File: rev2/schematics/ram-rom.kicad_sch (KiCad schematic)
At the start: 7 parts, among them U10 28C256, U11 28C256, U12 MT16D832

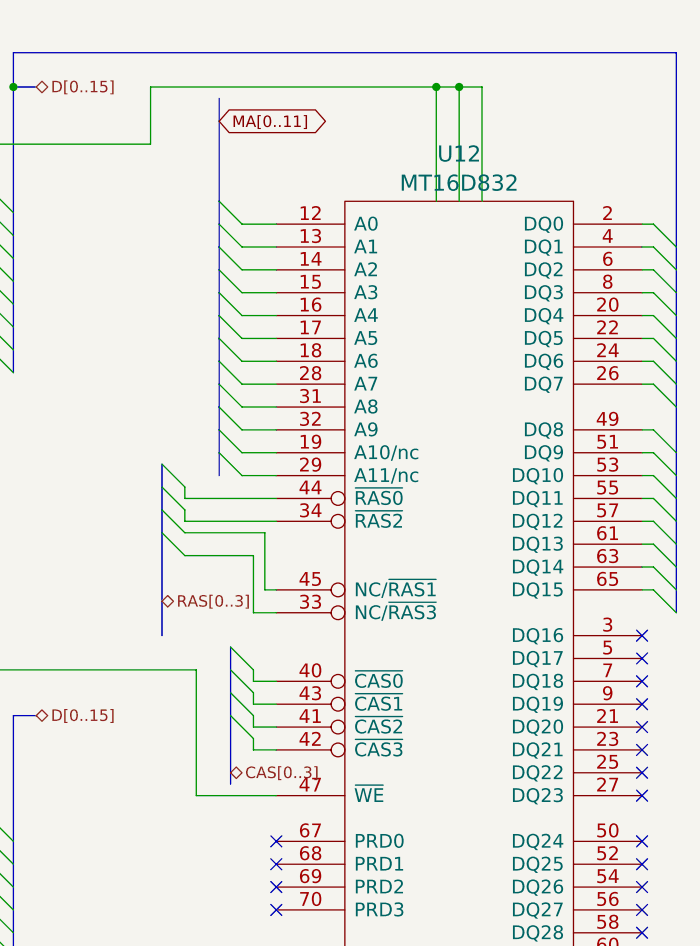
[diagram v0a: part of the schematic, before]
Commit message: Fixed Bus connections. Added SIMM control connections to the CPLD. Added missing symbols from rev1 library. Cleaned up some SRAM related control signals that are no longer needed.
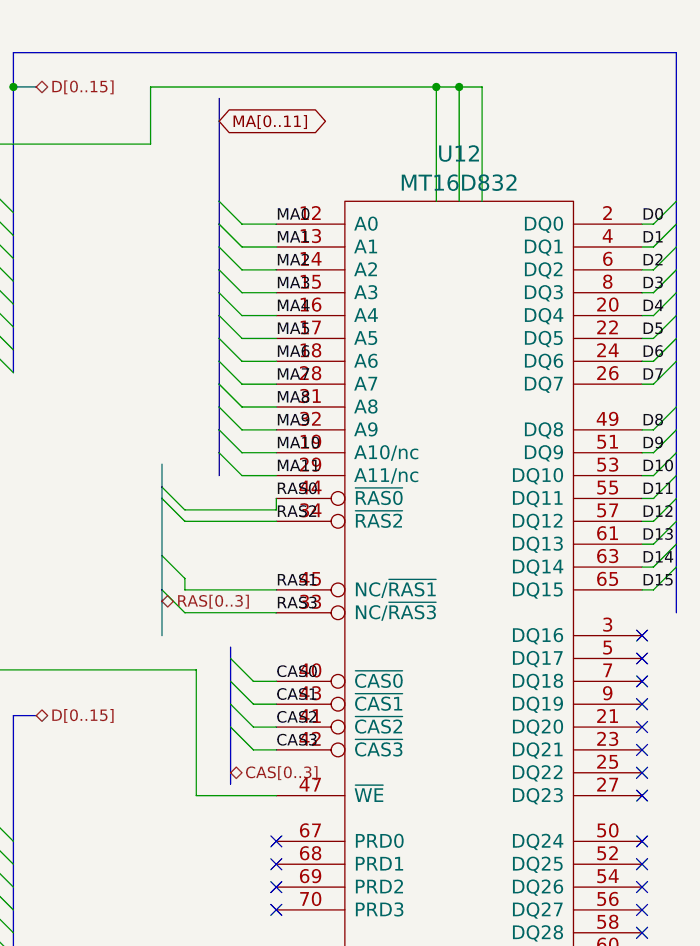
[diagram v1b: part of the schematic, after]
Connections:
- net D0: now also U12.2 (DQ0)
- net D1: now also U12.4 (DQ1)
- net D10: now also U12.53 (DQ10)
- net D11: now also U12.55 (DQ11)
- net D12: now also U12.57 (DQ12)
- net D13: now also U12.61 (DQ13)
- net D14: now also U12.63 (DQ14)
- net D15: now also U12.65 (DQ15)
- net D2: now also U12.6 (DQ2)
- net D3: now also U12.8 (DQ3)
- net D4: now also U12.20 (DQ4)
- net D5: now also U12.22 (DQ5)
- net D6: now also U12.24 (DQ6)
- net D7: now also U12.26 (DQ7)
- net D8: now also U12.49 (DQ8)
- net D9: now also U12.51 (DQ9)
- net MA0: now reaches U12.12 (A0)
- net MA1: now reaches U12.13 (A1)
- net MA2: now reaches U12.14 (A2)
- net MA3: now reaches U12.15 (A3)
- net MA4: now reaches U12.16 (A4)
- net MA5: now reaches U12.17 (A5)
- net MA6: now reaches U12.18 (A6)
- net MA10: now reaches U12.19 (A10/nc)
- net MA7: now reaches U12.28 (A7)
- net MA11: now reaches U12.29 (A11/nc)
- net MA8: now reaches U12.31 (A8)
- net MA9: now reaches U12.32 (A9)
- net RAS3: now reaches U12.33 (NC/~{RAS3})
- net RAS2: now reaches U12.34 (~{RAS2})
- net CAS0: now reaches U12.40 (~{CAS0})
- net CAS2: now reaches U12.41 (~{CAS2})
- net CAS3: now reaches U12.42 (~{CAS3})
- net CAS1: now reaches U12.43 (~{CAS1})
- net RAS0: now reaches U12.44 (~{RAS0})
- net RAS1: now reaches U12.45 (NC/~{RAS1})

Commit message: Added hierarchical labels from main sheet to RAM and ROM sheet.
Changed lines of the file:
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@@
     (effects (font (size 10.0076 10.0076)) (justify left bottom))
   )
-  (label "CAS2" (at 209.55 97.79 0)
+  (label "CAS2" (at 209.55 97.79 0) (fields_autoplaced)
     (effects (font (size 1.27 1.27)) (justify left bottom))
   )
@@
     (effects (font (size 1.27 1.27)) (justify left bottom))
   )
-  (label "MA8" (at 209.55 62.23 0)
+  (label "MA8" (at 209.55 62.23 0) (fields_autoplaced)
     (effects (font (size 1.27 1.27)) (justify left bottom))
   )
@@
     (effects (font (size 1.27 1.27)) (justify left bottom))
   )
-  (label "RAS0" (at 209.55 72.39 0)
-    (effects (font (size 1.27 1.27)) (justify left bottom))
-  )
-  (label "D3" (at 250.19 49.53 0)
-    (effects (font (size 1.27 1.27)) (justify left bottom))
-  )
-  (label "MA0" (at 209.55 41.91 0)
-    (effects (font (size 1.27 1.27)) (justify left bottom))
-  )
-  (label "D15" (at 250.19 82.55 0)
+  (label "RAS0" (at 209.55 72.39 0) (fields_autoplaced)
+    (effects (font (size 1.27 1.27)) (justify left bottom))
+  )
+  (label "D3" (at 250.19 49.53 0) (fields_autoplaced)
+    (effects (font (size 1.27 1.27)) (justify left bottom))
+  )
+  (label "MA0" (at 209.55 41.91 0) (fields_autoplaced)
+    (effects (font (size 1.27 1.27)) (justify left bottom))
+  )
+  (label "D15" (at 250.19 82.55 0) (fields_autoplaced)
     (effects (font (size 1.27 1.27)) (justify left bottom))
   )
@@
     (effects (font (size 1.27 1.27)) (justify left bottom))
   )
-  (label "MA1" (at 209.55 44.45 0)
+  (label "MA1" (at 209.55 44.45 0) (fields_autoplaced)
     (effects (font (size 1.27 1.27)) (justify left bottom))
   )
@@
     (effects (font (size 1.27 1.27)) (justify left bottom))
   )
-  (label "CAS3" (at 209.55 100.33 0)
+  (label "CAS3" (at 209.55 100.33 0) (fields_autoplaced)
     (effects (font (size 1.27 1.27)) (justify left bottom))
   )
@@
     (effects (font (size 1.27 1.27)) (justify left bottom))
   )
-  (label "MA10" (at 209.55 67.31 0)
+  (label "MA10" (at 209.55 67.31 0) (fields_autoplaced)
     (effects (font (size 1.27 1.27)) (justify left bottom))
   )
@@
     (effects (font (size 1.27 1.27)) (justify left bottom))
   )
-  (label "D14" (at 250.19 80.01 0)
-    (effects (font (size 1.27 1.27)) (justify left bottom))
-  )
-  (label "D12" (at 250.19 74.93 0)
+  (label "D14" (at 250.19 80.01 0) (fields_autoplaced)
+    (effects (font (size 1.27 1.27)) (justify left bottom))
+  )
+  (label "D12" (at 250.19 74.93 0) (fields_autoplaced)
     (effects (font (size 1.27 1.27)) (justify left bottom))
   )
@@
     (effects (font (size 1.27 1.27)) (justify left bottom))
   )
-  (label "D1" (at 250.19 44.45 0)
-    (effects (font (size 1.27 1.27)) (justify left bottom))
-  )
-  (label "D0" (at 250.19 41.91 0)
-    (effects (font (size 1.27 1.27)) (justify left bottom))
-  )
-  (label "MA6" (at 209.55 57.15 0)
+  (label "D1" (at 250.19 44.45 0) (fields_autoplaced)
+    (effects (font (size 1.27 1.27)) (justify left bottom))
+  )
+  (label "D0" (at 250.19 41.91 0) (fields_autoplaced)
+    (effects (font (size 1.27 1.27)) (justify left bottom))
+  )
+  (label "MA6" (at 209.55 57.15 0) (fields_autoplaced)
     (effects (font (size 1.27 1.27)) (justify left bottom))
   )
@@
     (effects (font (size 1.27 1.27)) (justify left bottom))
   )
-  (label "D6" (at 250.19 57.15 0)
-    (effects (font (size 1.27 1.27)) (justify left bottom))
-  )
-  (label "D10" (at 250.19 69.85 0)
-    (effects (font (size 1.27 1.27)) (justify left bottom))
-  )
-  (label "CAS1" (at 209.55 95.25 0)
-    (effects (font (size 1.27 1.27)) (justify left bottom))
-  )
-  (label "D9" (at 250.19 67.31 0)
-    (effects (font (size 1.27 1.27)) (justify left bottom))
-  )
-  (label "MA2" (at 209.55 46.99 0)
+  (label "D6" (at 250.19 57.15 0) (fields_autoplaced)
+    (effects (font (size 1.27 1.27)) (justify left bottom))
+  )
+  (label "D10" (at 250.19 69.85 0) (fields_autoplaced)
+    (effects (font (size 1.27 1.27)) (justify left bottom))
+  )
+  (label "CAS1" (at 209.55 95.25 0) (fields_autoplaced)
+    (effects (font (size 1.27 1.27)) (justify left bottom))
+  )
+  (label "D9" (at 250.19 67.31 0) (fields_autoplaced)
+    (effects (font (size 1.27 1.27)) (justify left bottom))
+  )
+  (label "MA2" (at 209.55 46.99 0) (fields_autoplaced)
     (effects (font (size 1.27 1.27)) (justify left bottom))
   )
@@
     (effects (font (size 1.27 1.27)) (justify left bottom))
   )
-  (label "D7" (at 250.19 59.69 0)
+  (label "D7" (at 250.19 59.69 0) (fields_autoplaced)
     (effects (font (size 1.27 1.27)) (justify left bottom))
   )
@@
     (effects (font (size 1.27 1.27)) (justify left bottom))
   )
-  (label "CAS0" (at 209.55 92.71 0)
-    (effects (font (size 1.27 1.27)) (justify left bottom))
-  )
-  (label "MA5" (at 209.55 54.61 0)
-    (effects (font (size 1.27 1.27)) (justify left bottom))
-  )
-  (label "MA7" (at 209.55 59.69 0)
+  (label "CAS0" (at 209.55 92.71 0) (fields_autoplaced)
+    (effects (font (size 1.27 1.27)) (justify left bottom))
+  )
+  (label "MA5" (at 209.55 54.61 0) (fields_autoplaced)
+    (effects (font (size 1.27 1.27)) (justify left bottom))
+  )
+  (label "MA7" (at 209.55 59.69 0) (fields_autoplaced)
     (effects (font (size 1.27 1.27)) (justify left bottom))
   )
@@
     (effects (font (size 1.27 1.27)) (justify left bottom))
   )
-  (label "D2" (at 250.19 46.99 0)
+  (label "D2" (at 250.19 46.99 0) (fields_autoplaced)
     (effects (font (size 1.27 1.27)) (justify left bottom))
   )
@@
     (effects (font (size 1.27 1.27)) (justify left bottom))
   )
-  (label "D8" (at 250.19 64.77 0)
+  (label "D8" (at 250.19 64.77 0) (fields_autoplaced)
     (effects (font (size 1.27 1.27)) (justify left bottom))
   )
@@
     (effects (font (size 1.27 1.27)) (justify left bottom))
   )
-  (label "D5" (at 250.19 54.61 0)
-    (effects (font (size 1.27 1.27)) (justify left bottom))
-  )
-  (label "D4" (at 250.19 52.07 0)
-    (effects (font (size 1.27 1.27)) (justify left bottom))
-  )
-  (label "MA11" (at 209.55 69.85 0)
+  (label "D5" (at 250.19 54.61 0) (fields_autoplaced)
+    (effects (font (size 1.27 1.27)) (justify left bottom))
+  )
+  (label "D4" (at 250.19 52.07 0) (fields_autoplaced)
+    (effects (font (size 1.27 1.27)) (justify left bottom))
+  )
+  (label "MA11" (at 209.55 69.85 0) (fields_autoplaced)
     (effects (font (size 1.27 1.27)) (justify left bottom))
   )
@@
     (effects (font (size 1.27 1.27)) (justify left bottom))
   )
-  (label "MA4" (at 209.55 52.07 0)
+  (label "MA4" (at 209.55 52.07 0) (fields_autoplaced)
     (effects (font (size 1.27 1.27)) (justify left bottom))
   )
@@
     (effects (font (size 1.27 1.27)) (justify left bottom))
   )
-  (label "D11" (at 250.19 72.39 0)
+  (label "D11" (at 250.19 72.39 0) (fields_autoplaced)
     (effects (font (size 1.27 1.27)) (justify left bottom))
   )
@@
     (effects (font (size 1.27 1.27)) (justify left bottom))
   )
-  (label "RAS3" (at 209.55 85.09 0)
+  (label "RAS3" (at 209.55 85.09 0) (fields_autoplaced)
     (effects (font (size 1.27 1.27)) (justify left bottom))
   )
@@
     (effects (font (size 1.27 1.27)) (justify left bottom))
   )
-  (label "MA9" (at 209.55 64.77 0)
+  (label "MA9" (at 209.55 64.77 0) (fields_autoplaced)
     (effects (font (size 1.27 1.27)) (justify left bottom))
   )
@@
     (effects (font (size 1.27 1.27)) (justify left bottom))
   )
-  (label "MA3" (at 209.55 49.53 0)
+  (label "MA3" (at 209.55 49.53 0) (fields_autoplaced)
     (effects (font (size 1.27 1.27)) (justify left bottom))
   )
@@
     (effects (font (size 1.27 1.27)) (justify left bottom))
   )
-  (label "RAS1" (at 209.55 82.55 0)
+  (label "RAS1" (at 209.55 82.55 0) (fields_autoplaced)
     (effects (font (size 1.27 1.27)) (justify left bottom))
   )
@@
     (effects (font (size 1.27 1.27)) (justify left bottom))
   )
-  (label "RAS2" (at 209.55 74.93 0)
+  (label "RAS2" (at 209.55 74.93 0) (fields_autoplaced)
     (effects (font (size 1.27 1.27)) (justify left bottom))
   )
@@
     (effects (font (size 1.27 1.27)) (justify left bottom))
   )
-  (label "D13" (at 250.19 77.47 0)
+  (label "D13" (at 250.19 77.47 0) (fields_autoplaced)
     (effects (font (size 1.27 1.27)) (justify left bottom))
   )
@@
     (effects (font (size 1.27 1.27)) (justify right))
   )
+  (hierarchical_label "MA[0..11]" (shape input) (at 203.2 33.02 0) (fields_autoplaced)
+    (effects (font (size 1.27 1.27)) (justify left))
+  )
   (hierarchical_label "~{WE}" (shape input) (at 80.01 71.12 0) (fields_autoplaced)

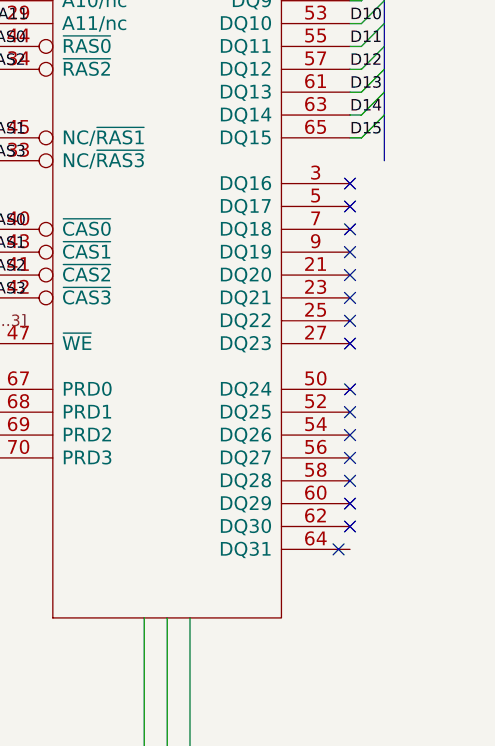
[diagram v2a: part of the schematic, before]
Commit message: Added upper two bytes to SIMM connection. Updated the PCB at the same time.
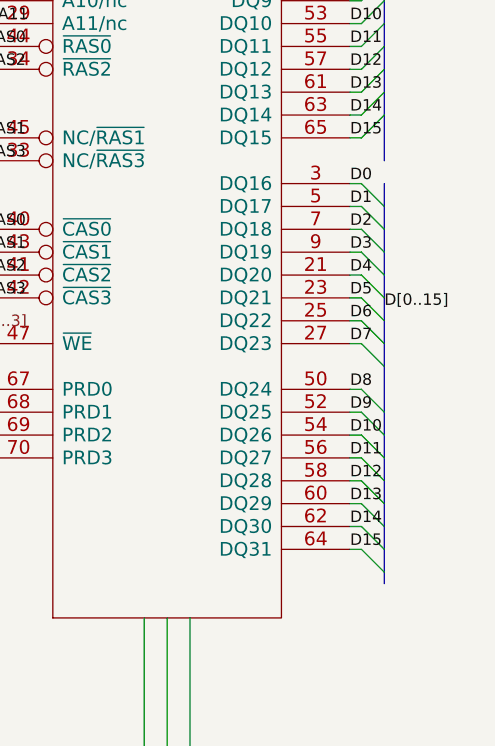
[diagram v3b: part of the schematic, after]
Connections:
- net D0: now also U12.3 (DQ16)
- net D1: now also U12.5 (DQ17)
- net D10: now also U12.54 (DQ26)
- net D11: now also U12.56 (DQ27)
- net D12: now also U12.58 (DQ28)
- net D13: now also U12.60 (DQ29)
- net D14: now also U12.62 (DQ30)
- net D15: now also U12.64 (DQ31)
- net D2: now also U12.7 (DQ18)
- net D3: now also U12.9 (DQ19)
- net D4: now also U12.21 (DQ20)
- net D5: now also U12.23 (DQ21)
- net D6: now also U12.25 (DQ22)
- net D7: now also U12.27 (DQ23)
- net D8: now also U12.50 (DQ24)
- net D9: now also U12.52 (DQ25)
- no-connect marks 20 -> 4
